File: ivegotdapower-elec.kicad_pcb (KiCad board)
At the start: 2 copper layers, 87 x 70 mm, 74 parts, among them J1 Conn_Debug, J10 Conn_+3.3V, J11 Conn_bau, J12 CAN_conn, J13 CAN_conn, J2 Conn_batt, J3 Conn_alim, J4 Conn_TSMR, J5 Conn_POW2, J6 Conn_POW1, J7 Conn_RPi, J8 Conn_+5V, Q1 IRFR5305, Q2 IRFR5305, Q3 BSS138, Q4 MMBT2907A, Q5 MMBT2907A, Q6 MMBT2907A, Q7 MMBT2907A, U1 TCAN332, U10 LD1117S33TR_SOT223, U11 LM358, U6 ACS711xLCTR-12AB, U7 STM32F303K8Tx, U8 LD1117S50TR_SOT223

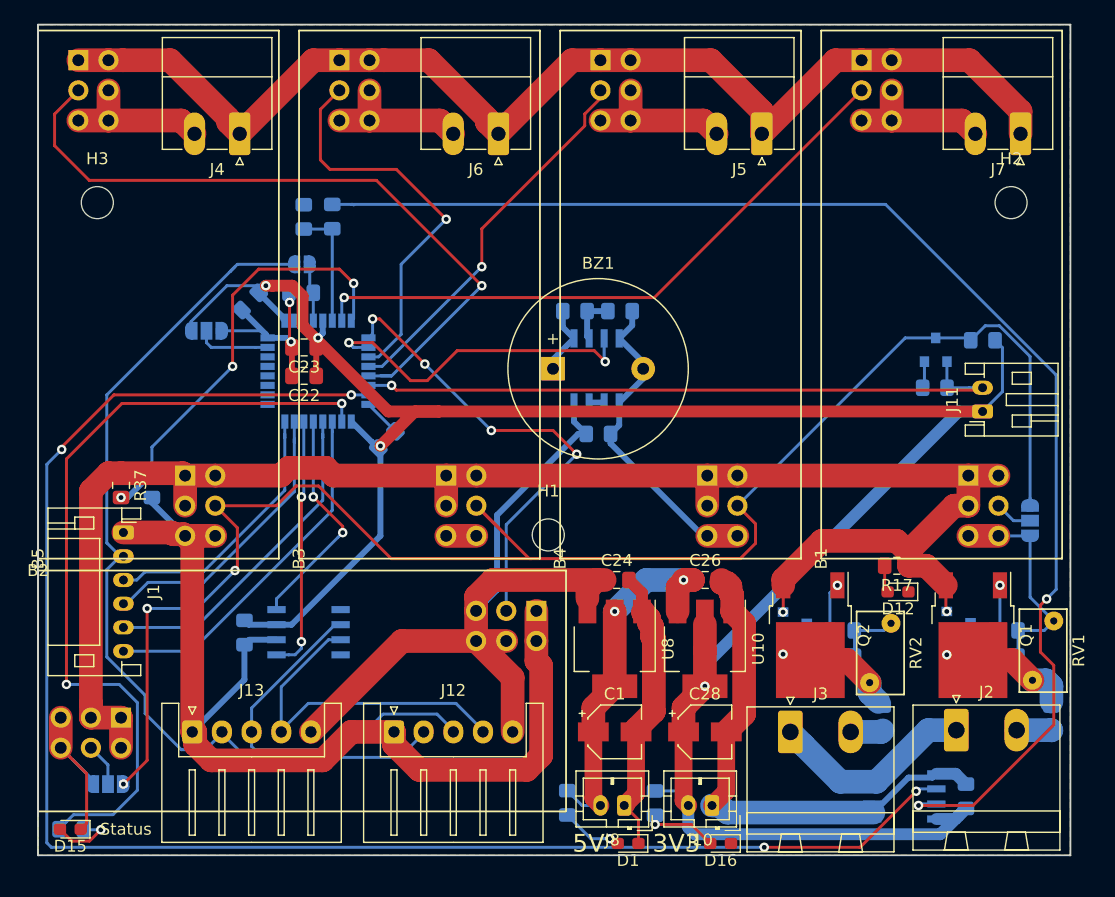
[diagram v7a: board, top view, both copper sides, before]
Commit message: Improvements on GND nets
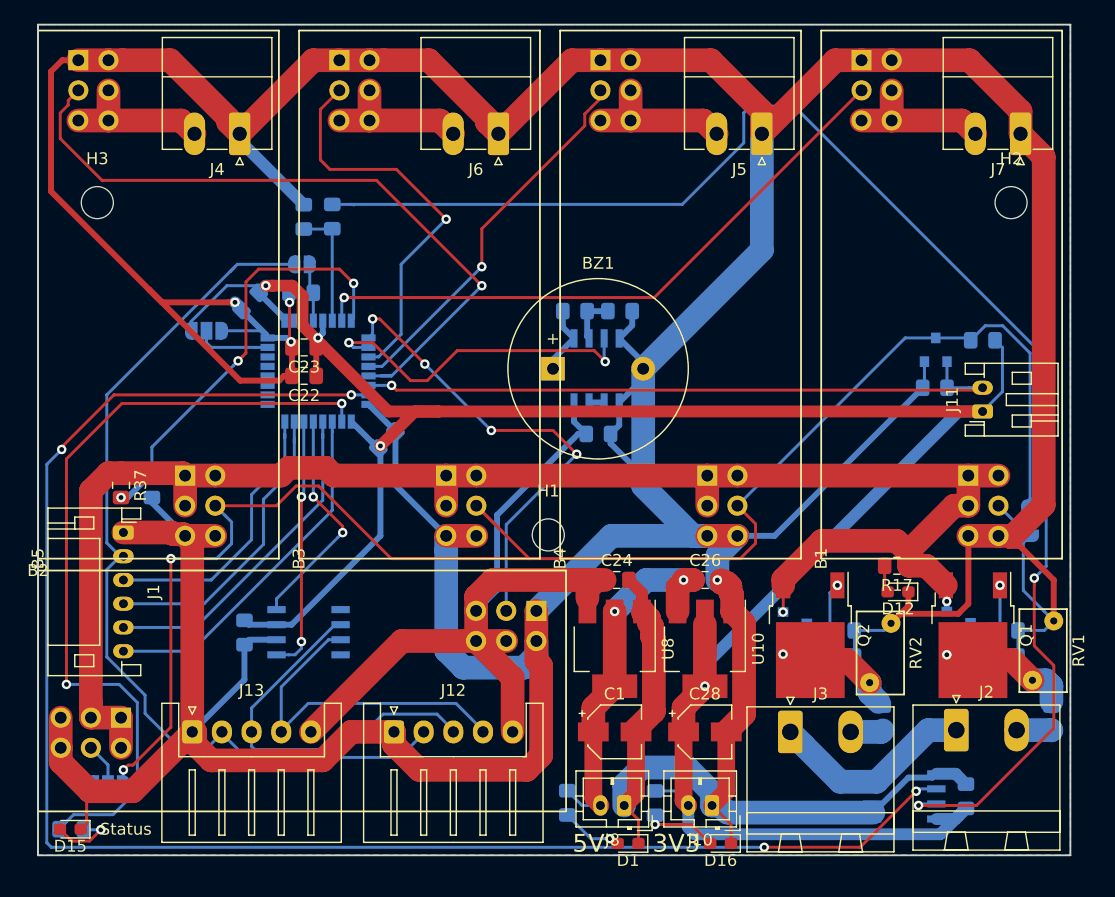
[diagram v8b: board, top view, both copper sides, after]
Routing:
- net GND: track 351.0 -> 618.1 mm, vias 2 -> 4
- net /STM32/sense: track 113.4 -> 122.0 mm
- net /STM32/TMS: track 24.5 -> 25.6 mm
- net /STM32/TSMR: track 60.0 -> 59.0 mm
- net /STM32/TCK: track 22.8 -> 23.6 mm
- net /buck/on-off: track 138.2 -> 138.0 mm, vias 3 -> 2
